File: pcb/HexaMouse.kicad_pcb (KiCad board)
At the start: 2 copper layers, 55 x 55 mm, 23 parts, among them J1 Conn_01x02_Socket, J2 Conn_01x02_Socket, J3 Xiao_Headers_Left, J4 Xiao_Headers_Right, SW1 SW_SPDT, U2 TLV493D, U3 TLV493D, U4 TLV493D, U5 TCA9548APWR

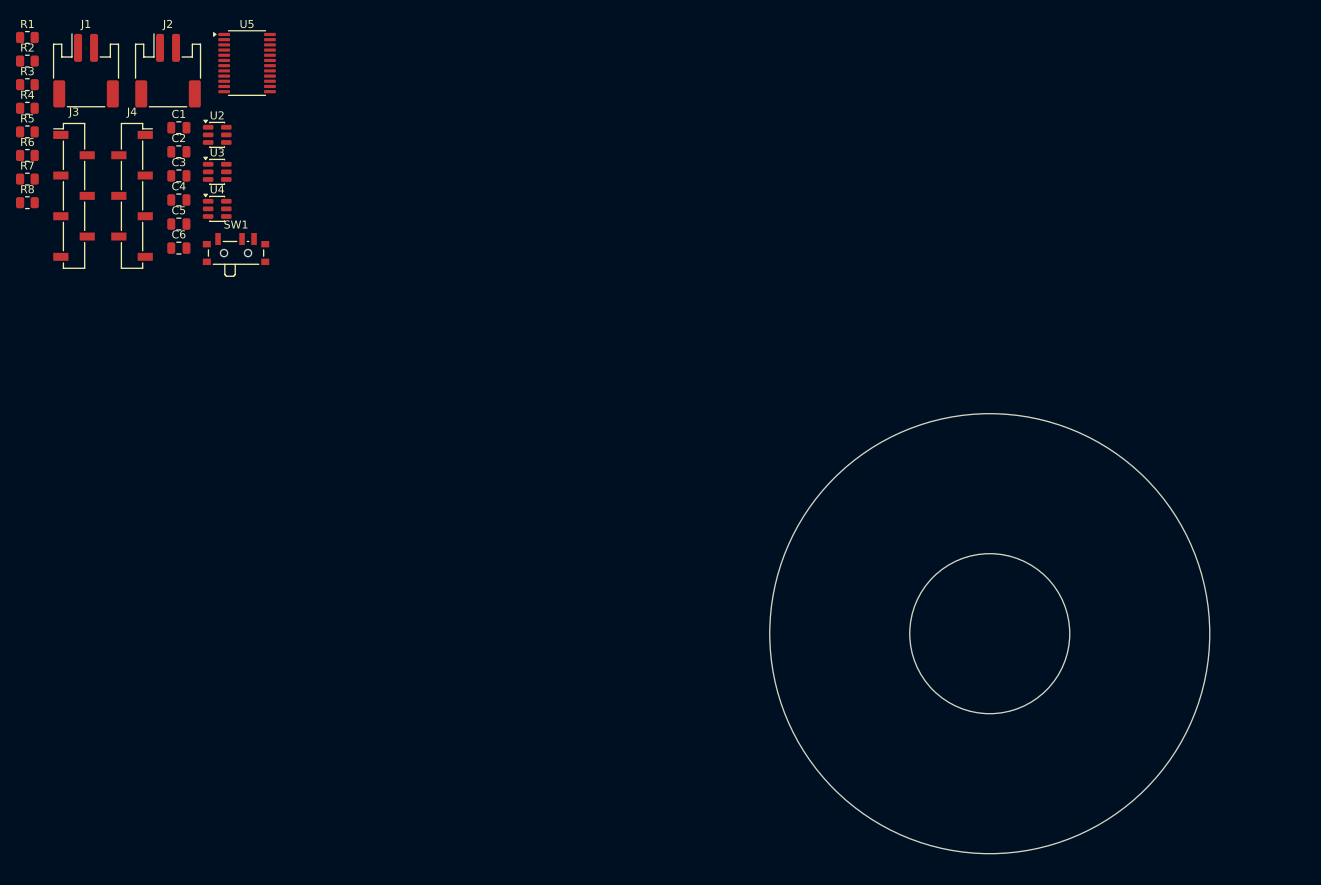
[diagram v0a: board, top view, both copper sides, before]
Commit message: Fixed pcb shape and positioned pos sensitive components
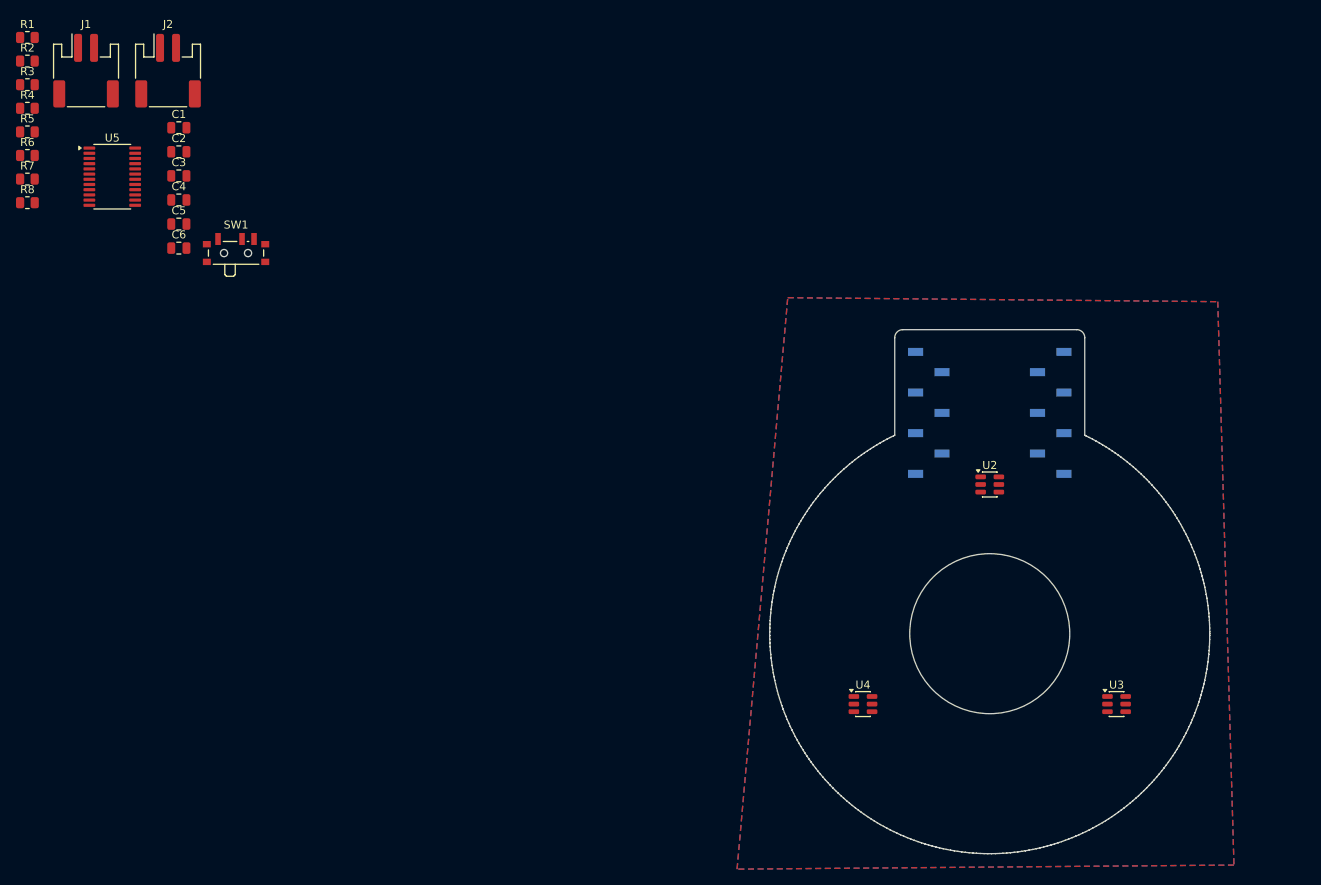
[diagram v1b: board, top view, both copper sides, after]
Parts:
- J3, J4: moved to B.Cu
- moved U3 130.6 mm to (165.8, 108.8)
- moved J3 125.1 mm to (157.6, 72.4), turned to 180 degrees
- moved U2 106.0 mm to (150.0, 81.3)
- moved J4 103.2 mm to (142.4, 72.4), turned to 180 degrees
- moved U4 101.7 mm to (134.2, 108.8)
- moved U5 22.0 mm to (40.3, 42.9)
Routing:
- added copper zone on B.Cu, net GND
- added copper zone on F.Cu, net GND
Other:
- board size 55 x 55 mm -> 55 x 65.5 mm

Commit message: Swapped jst connector footprint, and positioned some more components
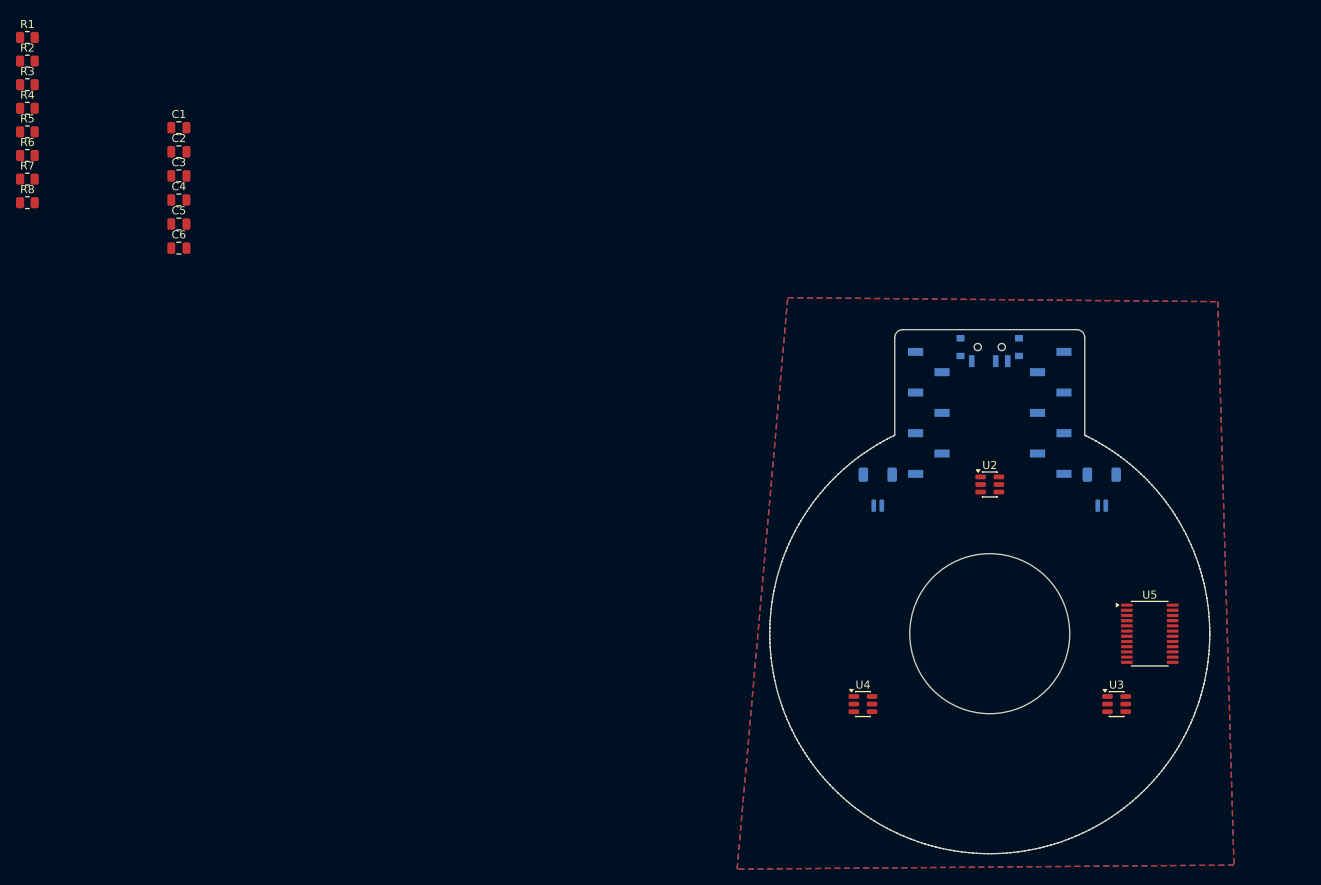
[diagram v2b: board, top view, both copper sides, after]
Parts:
- J1, J2: footprint Connector_JST:JST_PH_S2B-PH-SM4-TB_1x02-1MP_P2.00mm_Horizontal -> Connector_JST:JST_SH_SM02B-SRSS-TB_1x02-1MP_P1.00mm_Horizontal; moved to B.Cu
- SW1: moved to B.Cu
- moved U5 141.7 mm to (170.0, 100.0)
- moved J2 127.9 mm to (164.0, 82.0)
- moved J1 112.0 mm to (136.0, 82.0)
- moved SW1 95.0 mm to (150.0, 64.5)

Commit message: Added and positioned mounting holes
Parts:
- added H1: MountingHole, MountingHole:MountingHole_3.2mm_M3, F.Cu at (134.2, 90.9)
- added H2: MountingHole, MountingHole:MountingHole_3.2mm_M3, F.Cu at (165.8, 90.9)
- added H3: MountingHole, MountingHole:MountingHole_3.2mm_M3, F.Cu at (150.0, 118.3)

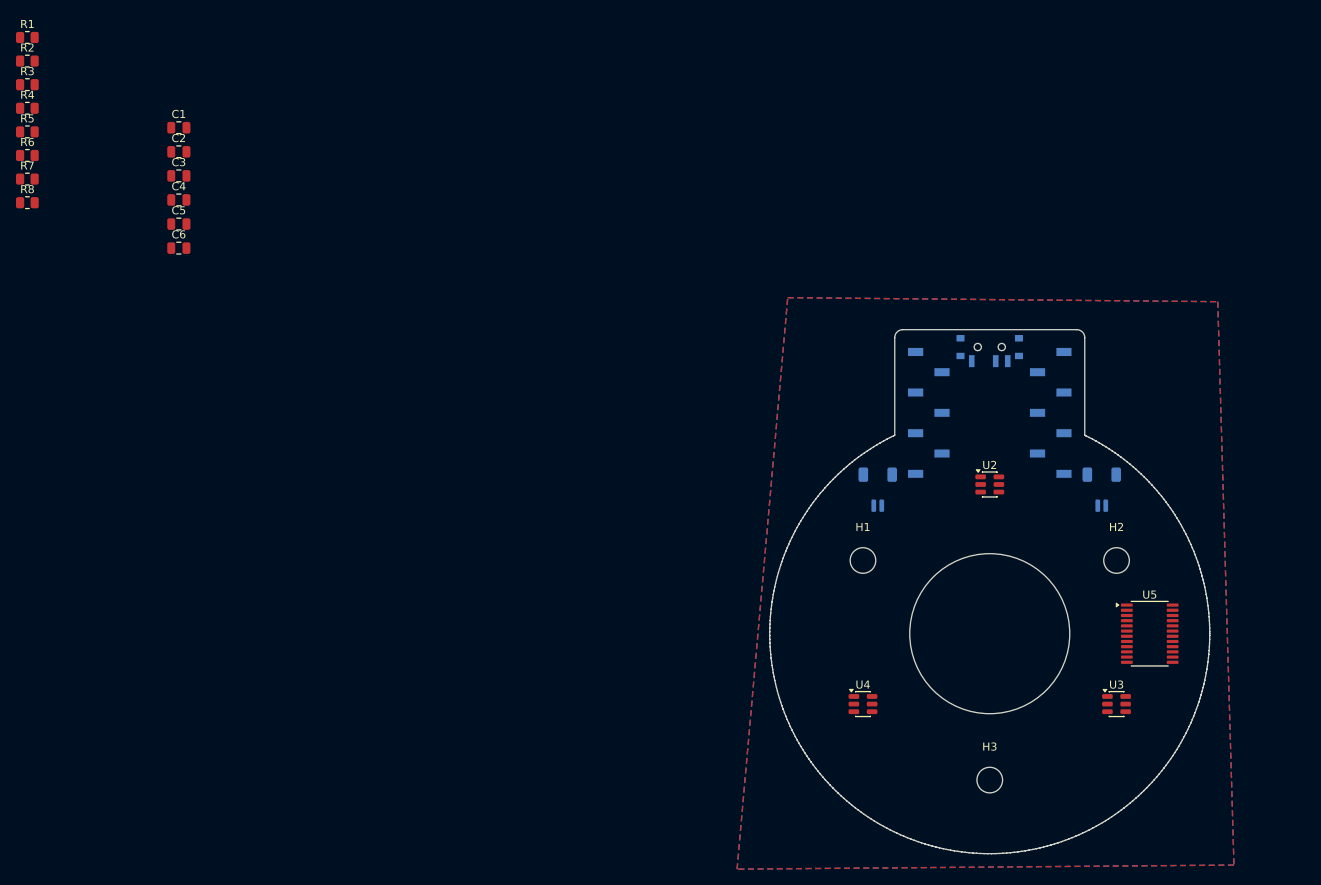
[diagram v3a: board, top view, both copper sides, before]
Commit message: Positioned all capacitors
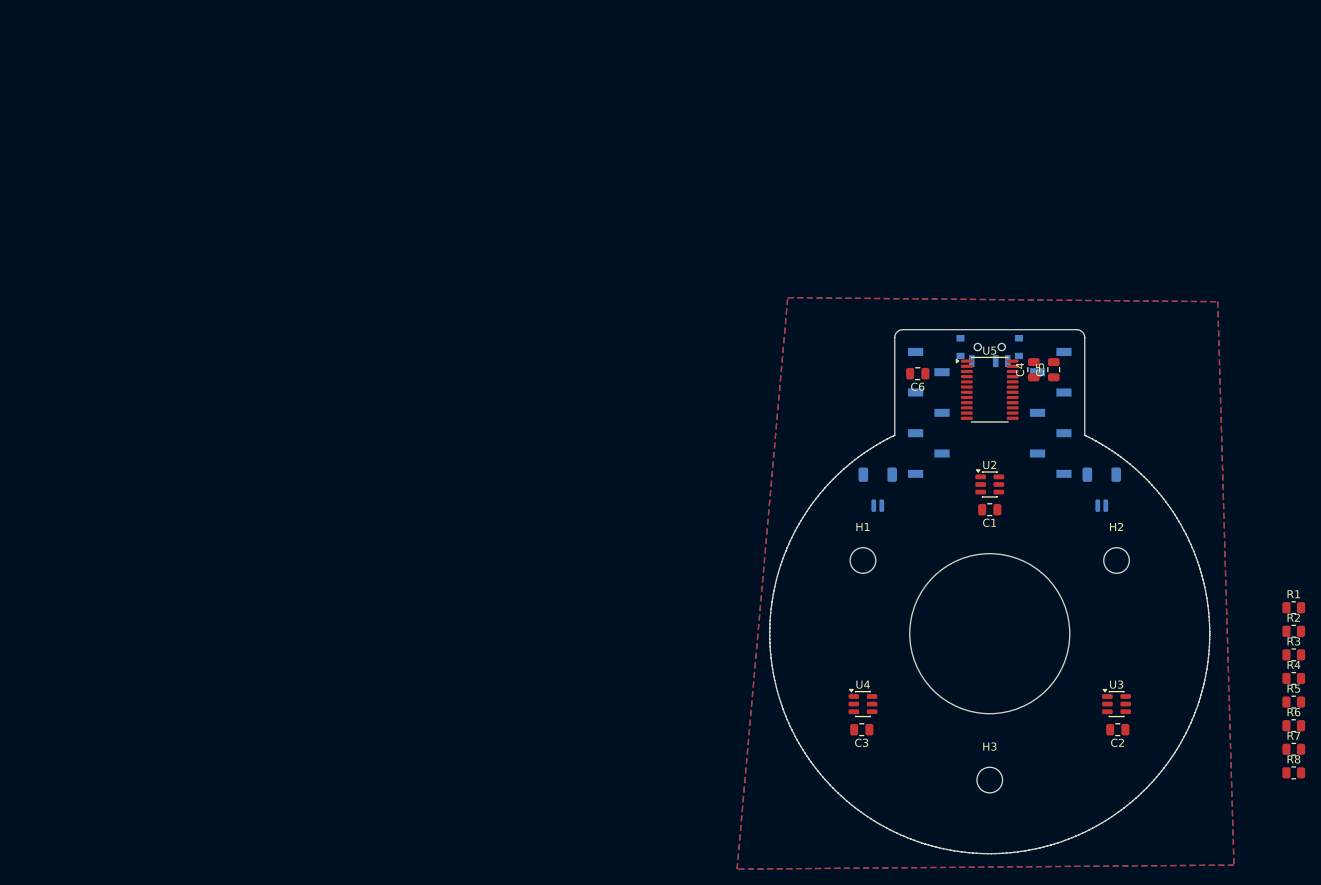
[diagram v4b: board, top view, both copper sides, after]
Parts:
- moved R1 173.6 mm to (188.0, 96.8)
- moved R2 173.6 mm to (188.0, 99.7)
- moved R3 173.6 mm to (188.0, 102.7)
- moved R4 173.6 mm to (188.0, 105.6)
- moved R5 173.6 mm to (188.0, 108.5)
- moved R6 173.6 mm to (188.0, 111.5)
- moved R7 173.6 mm to (188.0, 114.5)
- moved R8 173.6 mm to (188.0, 117.4)
- moved C2 137.8 mm to (166.0, 112.0), turned to 180 degrees
- moved C1 112.0 mm to (150.0, 84.5), turned to 180 degrees
- moved C5 110.9 mm to (158.0, 67.0), turned to 90 degrees
- moved C3 109.9 mm to (134.0, 112.0), turned to 180 degrees
- moved C4 109.0 mm to (155.5, 67.0), turned to 90 degrees
- moved C6 93.7 mm to (141.0, 67.5), turned to 180 degrees
- moved U5 36.5 mm to (150.0, 69.5)

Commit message: Positioned the resistors
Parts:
- moved R7 55.8 mm to (133.0, 105.0), turned to -90 degrees
- moved R8 53.9 mm to (135.5, 105.0), turned to -90 degrees
- moved R3 46.4 mm to (149.0, 77.5), turned to -90 degrees
- moved R4 46.1 mm to (151.5, 77.5), turned to -90 degrees
- moved R1 39.9 mm to (157.5, 71.0), turned to 90 degrees
- moved R2 39.2 mm to (157.5, 75.0), turned to 90 degrees
- moved R5 23.8 mm to (164.5, 105.0), turned to -90 degrees
- moved R6 22.0 mm to (167.0, 105.0), turned to -90 degrees
- moved C4 2.00 mm to (157.5, 67.0)
- moved C5 2.00 mm to (160.0, 67.0)

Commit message: Did pcb routing
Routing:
- net +3.3V: track 0.00 -> 128.4 mm, vias 0 -> 1
- net SD1: track 0.00 -> 59.8 mm, vias 0 -> 4
- net SC1: track 0.00 -> 52.8 mm, vias 0 -> 6
- net SC2: track 0.00 -> 50.4 mm, vias 0 -> 2
- net SD2: track 0.00 -> 44.3 mm, vias 0 -> 4
- net Net-(J2-Pin_2): track 0.00 -> 32.0 mm, vias 0 -> 2
- net Net-(J1-Pin_2): track 0.00 -> 30.3 mm
- net Net-(J1-Pin_1): track 0.00 -> 28.4 mm
- net SD0: track 0.00 -> 19.6 mm
- net SCL-MUX: track 0.00 -> 17.8 mm, vias 0 -> 3
- net SC0: track 0.00 -> 17.6 mm, vias 0 -> 2
- net SDA-MUX: track 0.00 -> 12.3 mm, vias 0 -> 1
- net GND: track 0.00 -> 9.93 mm, vias 0 -> 15

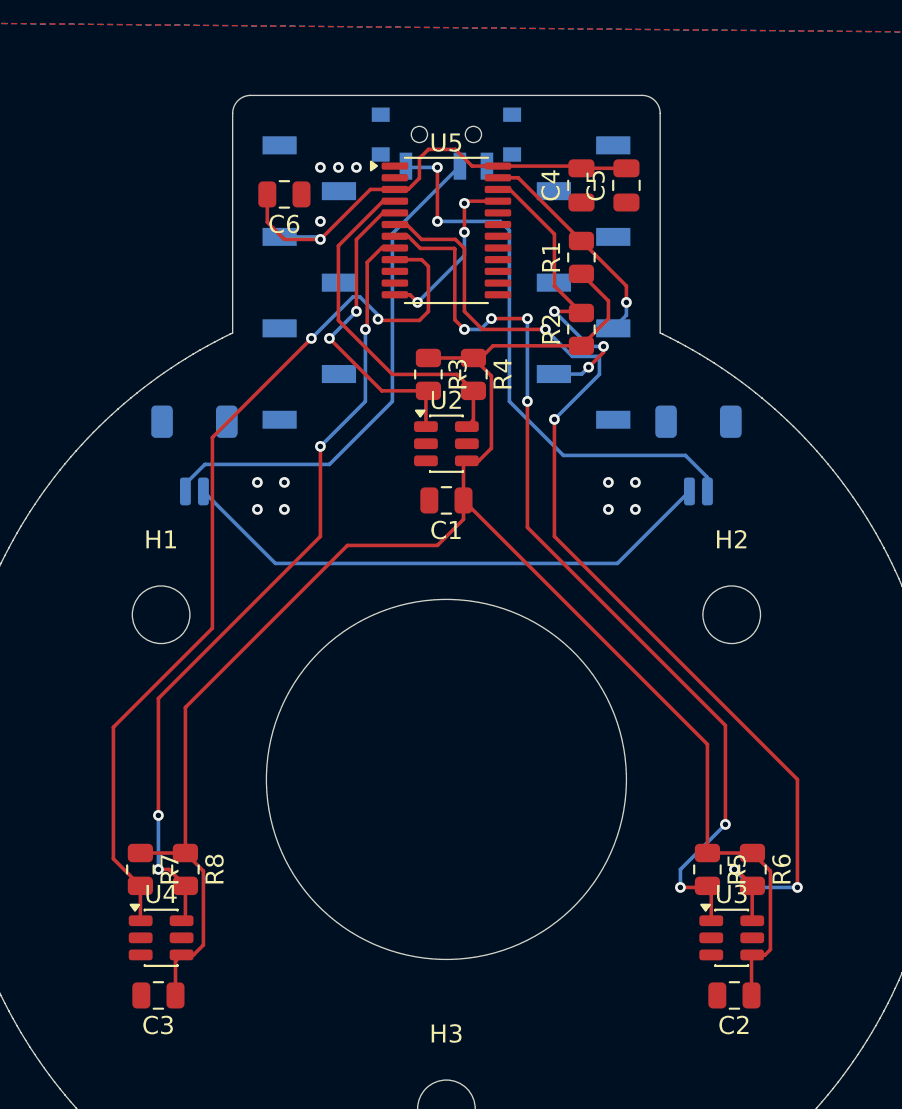
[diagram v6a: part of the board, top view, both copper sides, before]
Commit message: Did some ground stitching
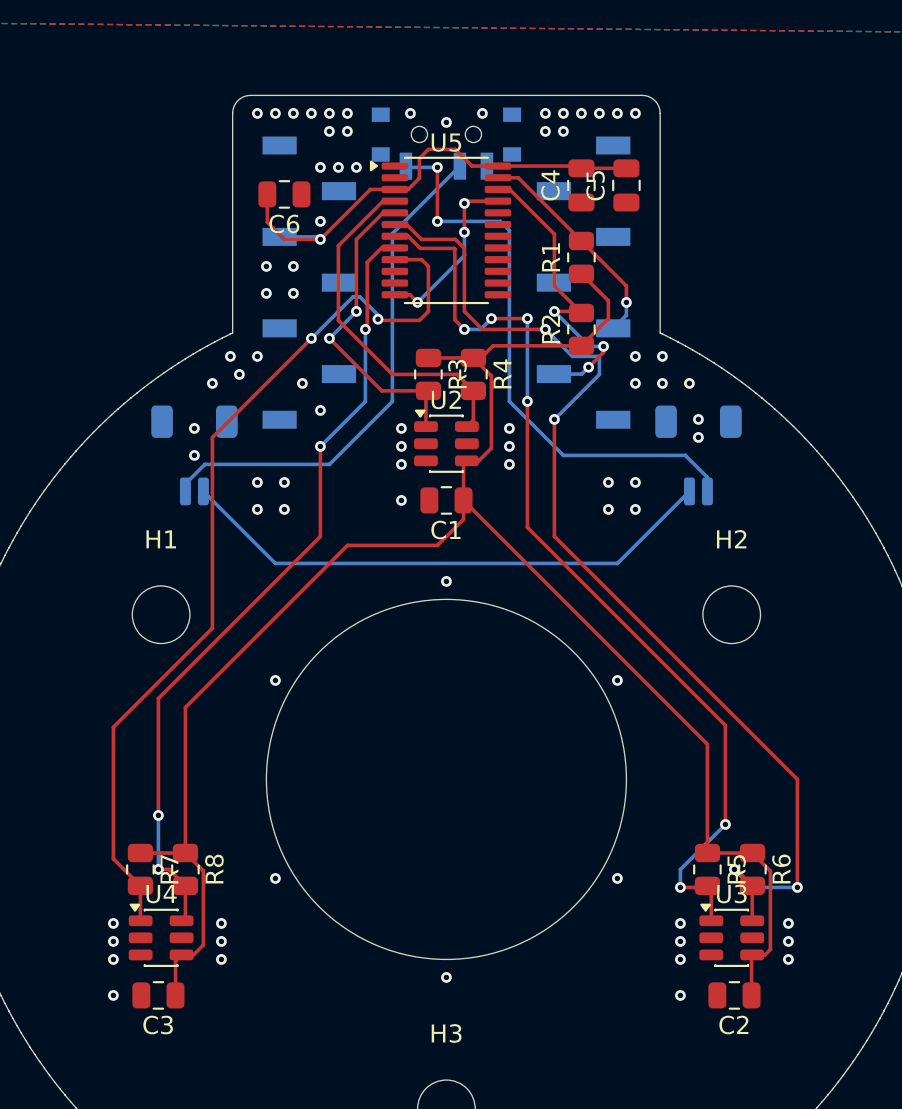
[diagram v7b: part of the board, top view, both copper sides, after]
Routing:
- net GND: vias 15 -> 80

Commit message: Fixed DRC issues
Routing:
- net GND: track 9.93 -> 33.5 mm, vias 80 -> 83
- net +3.3V: track 128.4 -> 138.7 mm
